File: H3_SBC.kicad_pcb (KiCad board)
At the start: 2 copper layers, 50 x 40 mm, 11 parts, among them CN1 YXT-BB10-50P-02, CN2 YXT-BB10-50P-02, CN3 YXT-BB10-50P-02, J1 HR911105A_C12074, U1 H3, U2 AXP223_C2997893, U3 K4B4G1646E-BYMA 4GB, U4 K4B4G1646E-BYMA 4GB, U5 KLM4G1FETE-B041, U8 XOS32024000LT00351005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

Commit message: changed some ethernet stuff
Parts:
- removed J1: HR911105A_C12074, easyeda2kicad:RJ45-TH_HR911105A
- added RJ1: R-RJ45R08P-C000, easyeda2kicad:RJ45-TH_R-RJ45R08P-C000, F.Cu at (212.5, 79.1)
- added U9: RTL8211E-VB-CG, easyeda2kicad:QFN-48_L6.0-W6.0-P0.40-BL-EP3.8, F.Cu at (190.3, 92.1)
- moved U1 0.14 mm to (176.0, 86.9)
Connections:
- CN2 pad 1: unconnected-(CN2-Pad1) -> ENET_MDI0+
- CN2 pad 10: unconnected-(CN2-Pad10) -> ENET_MDI3+
- CN2 pad 11: unconnected-(CN2-Pad11) -> ENET_MDI3-
- CN2 pad 12: unconnected-(CN2-Pad12) -> GND
- CN2 pad 13: unconnected-(CN2-Pad13) -> ENET_LED1
- CN2 pad 14: unconnected-(CN2-Pad14) -> ENET_LED0
- CN2 pad 15: unconnected-(CN2-Pad15) -> ENET_LED2
- CN2 pad 16: unconnected-(CN2-Pad16) -> GND
- CN2 pad 2: unconnected-(CN2-Pad2) -> ENET_MDI0-
- CN2 pad 3: unconnected-(CN2-Pad3) -> GND
- CN2 pad 4: unconnected-(CN2-Pad4) -> ENET_MDI1+
- CN2 pad 5: unconnected-(CN2-Pad5) -> ENET_MDI1-
- CN2 pad 6: unconnected-(CN2-Pad6) -> GND
- CN2 pad 7: unconnected-(CN2-Pad7) -> ENET_MDI2+
- CN2 pad 8: unconnected-(CN2-Pad8) -> ENET_MDI2-
- CN2 pad 9: unconnected-(CN2-Pad9) -> GND
- CN3 pad 1: unconnected-(CN3-Pad1) -> JTAG_MS
- CN3 pad 10: unconnected-(CN3-Pad10) -> GND
- CN3 pad 11: unconnected-(CN3-Pad11) -> PA8
- CN3 pad 12: unconnected-(CN3-Pad12) -> PA9
- CN3 pad 13: unconnected-(CN3-Pad13) -> PA10
- CN3 pad 14: unconnected-(CN3-Pad14) -> GND
- CN3 pad 15: unconnected-(CN3-Pad15) -> TWI0_SCK
- CN3 pad 16: unconnected-(CN3-Pad16) -> TWI0_SDA
- CN3 pad 17: unconnected-(CN3-Pad17) -> GND
- CN3 pad 18: unconnected-(CN3-Pad18) -> UART3_TX
- CN3 pad 19: unconnected-(CN3-Pad19) -> UART3_RX
- CN3 pad 2: unconnected-(CN3-Pad2) -> JTAG_CK
- CN3 pad 20: unconnected-(CN3-Pad20) -> UART3_RTS
- CN3 pad 21: unconnected-(CN3-Pad21) -> UART3_CTS
- CN3 pad 3: unconnected-(CN3-Pad3) -> JTAG_DO
- CN3 pad 4: unconnected-(CN3-Pad4) -> JTAG_DI
- CN3 pad 41: unconnected-(CN3-Pad41) -> SPI0_CS
- CN3 pad 42: unconnected-(CN3-Pad42) -> SPI0_CLK
- CN3 pad 43: unconnected-(CN3-Pad43) -> SPI0_MISO
- CN3 pad 44: unconnected-(CN3-Pad44) -> SPI0_MOSI
- CN3 pad 45: unconnected-(CN3-Pad45) -> GND
- CN3 pad 46: unconnected-(CN3-Pad46) -> PA21
- CN3 pad 47: unconnected-(CN3-Pad47) -> PA20
- CN3 pad 48: unconnected-(CN3-Pad48) -> PA19
- CN3 pad 49: unconnected-(CN3-Pad49) -> PA18
- CN3 pad 5: unconnected-(CN3-Pad5) -> GND
- CN3 pad 50: unconnected-(CN3-Pad50) -> PA17
- CN3 pad 6: unconnected-(CN3-Pad6) -> PA4
- CN3 pad 7: unconnected-(CN3-Pad7) -> PA5
- CN3 pad 8: unconnected-(CN3-Pad8) -> PA6
- CN3 pad 9: unconnected-(CN3-Pad9) -> PA7
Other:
- copper layers 2 -> 6

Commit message: switched eMMC
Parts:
- removed U5: KLM4G1FETE-B041, easyeda2kicad:FBGA-153_L11.0-W10.0-P0.50_KLM4G1FETE-B041
- added U10: XT28EG32GA4YJECGA, easyeda2kicad:VFBGA-153_L13.0-W11.5-P0.50-BL_SKYHIGHMEMORY_S40FC004C1B1I00000, F.Cu at (176.2, 72.3)

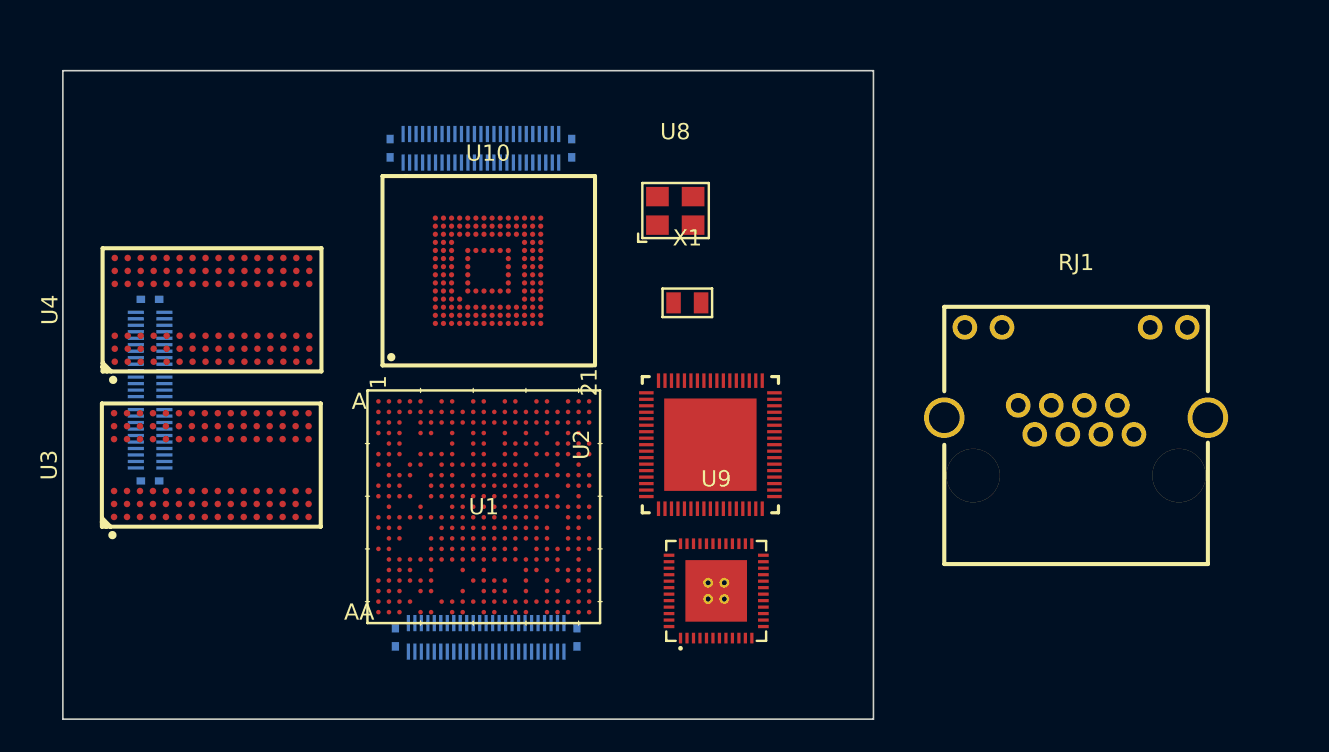
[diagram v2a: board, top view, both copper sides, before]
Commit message: power changes and pinout update
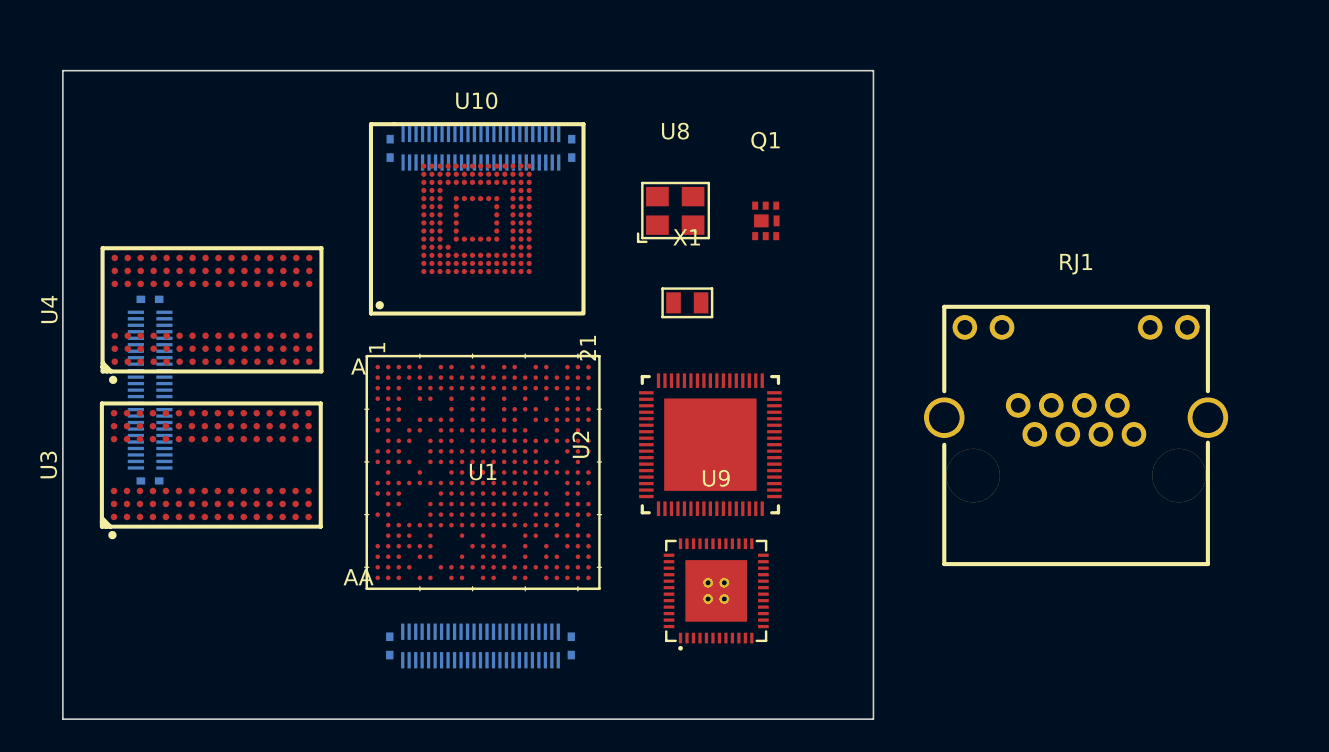
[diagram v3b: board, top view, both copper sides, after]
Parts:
- added Q1: WPM1481-6/TR, easyeda2kicad:DFN-6L_L2.0-W2.0-P0.65-BL_WPM1481-6, F.Cu at (193.4, 69.3)
- moved U10 3.28 mm to (175.5, 69.1)
- moved U1 2.12 mm to (175.9, 84.8)
- moved CN2 0.64 mm to (175.8, 95.5)
- turned CN1 to 0 degrees
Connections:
- CN1 pad 26: unconnected-(CN1-Pad26) -> CHG_LED
- CN1 pad 27: unconnected-(CN1-Pad27) -> PWR_ON
- CN1 pad 28: unconnected-(CN1-Pad28) -> GND
- CN2 pad 41: unconnected-(CN2-Pad41) -> SPI0_CS
- CN2 pad 42: unconnected-(CN2-Pad42) -> SPI0_CLK
- CN2 pad 43: unconnected-(CN2-Pad43) -> SPI0_MISO
- CN2 pad 44: unconnected-(CN2-Pad44) -> SPI0_MOSI
- CN2 pad 45: unconnected-(CN2-Pad45) -> GND
- CN2 pad 46: unconnected-(CN2-Pad46) -> PA21
- CN2 pad 47: unconnected-(CN2-Pad47) -> PA20
- CN2 pad 48: unconnected-(CN2-Pad48) -> PA19
- CN2 pad 49: unconnected-(CN2-Pad49) -> PA18
- CN2 pad 50: unconnected-(CN2-Pad50) -> PA17
- CN3 pad 26: unconnected-(CN3-Pad26) -> AXP_PWROK
- CN3 pad 27: unconnected-(CN3-Pad27) -> PWR_ON
- CN3 pad 28: unconnected-(CN3-Pad28) -> ELDO3
- CN3 pad 29: unconnected-(CN3-Pad29) -> ELDO3
- CN3 pad 30: unconnected-(CN3-Pad30) -> ELDO2
- CN3 pad 31: unconnected-(CN3-Pad31) -> ELDO2
- CN3 pad 32: unconnected-(CN3-Pad32) -> ELDO1
- CN3 pad 33: unconnected-(CN3-Pad33) -> ELDO1
- CN3 pad 34: unconnected-(CN3-Pad34) -> NTC
- CN3 pad 35: unconnected-(CN3-Pad35) -> DLDO4
- CN3 pad 36: unconnected-(CN3-Pad36) -> DLDO4
- CN3 pad 37: unconnected-(CN3-Pad37) -> DLDO3
- CN3 pad 38: unconnected-(CN3-Pad38) -> DLDO3
- CN3 pad 39: unconnected-(CN3-Pad39) -> DLDO2
- CN3 pad 40: unconnected-(CN3-Pad40) -> DLDO2
- CN3 pad 41: SPI0_CS -> DLDO1
- CN3 pad 42: SPI0_CLK -> DLDO1
- CN3 pad 43: SPI0_MISO -> +BATT
- CN3 pad 44: SPI0_MOSI -> +BATT
- CN3 pad 45: GND -> +BATT
- CN3 pad 46: PA21 -> +BATT
- CN3 pad 47: PA20 -> +5V
- CN3 pad 48: PA19 -> +5V
- CN3 pad 49: PA18 -> +5V
- CN3 pad 50: PA17 -> +5V
- U2 pad 1: unconnected-(U2A-ELDOIN-Pad1) -> /Power/IPSOUT
- U2 pad 11: unconnected-(U2A-N_VBUSEN-Pad11) -> VCC_RTC
- U2 pad 12: unconnected-(U2A-PWRON-Pad12) -> PWR_ON
- U2 pad 13: Net-(U2B-VIN1) -> /Power/IPSOUT
- U2 pad 18: unconnected-(U2A-DLDOIN-Pad18) -> /Power/IPSOUT
- U2 pad 2: unconnected-(U2A-ELDO2-Pad2) -> ELDO2
- U2 pad 23: Net-(U2C-VIN2) -> /Power/IPSOUT
- U2 pad 29: unconnected-(U2A-IRQ-Pad29) -> AXP_IRQ
- U2 pad 3: unconnected-(U2A-ELDO3-Pad3) -> ELDO3
- U2 pad 30: unconnected-(U2A-TS-Pad30) -> NTC
- U2 pad 31: unconnected-(U2A-GPIO1/PWREN-Pad31) -> Net-(U2A-GPIO1/PWREN)
- U2 pad 32: unconnected-(U2A-ALDO1-Pad32) -> VCC_3V3_ANALOG
- U2 pad 33: unconnected-(U2A-ALDOIN-Pad33) -> /Power/IPSOUT
- U2 pad 37: unconnected-(U2A-GPIO0-Pad37) -> Net-(U2A-GPIO0)
- U2 pad 39: Net-(U2D-VIN3) -> /Power/IPSOUT
- U2 pad 43: unconnected-(U2A-PWROK-Pad43) -> AXP_PWROK
- U2 pad 44: unconnected-(U2A-SCK-Pad44) -> AXP_SCL
- U2 pad 45: unconnected-(U2A-SDA-Pad45) -> AXP_SDA
- U2 pad 46: Net-(U2A-VCC_RTC) -> VCC_RTC
- U2 pad 49: unconnected-(U2A-BATSENCE-Pad49) -> +BATT
- U2 pad 50: unconnected-(U2A-LOADSENCE-Pad50) -> /Power/CHSENCEN
- U2 pad 51: unconnected-(U2A-N_BATDRV-Pad51) -> /Power/N_BATDRV
- U2 pad 52: unconnected-(U2A-CHGLED-Pad52) -> CHG_LED
- U2 pad 53: unconnected-(U2A-PS-Pad53) -> /Power/IPSOUT
- U2 pad 54: unconnected-(U2A-PS-Pad54) -> /Power/IPSOUT
- U2 pad 57: unconnected-(U2A-CHSENCEP-Pad57) -> /Power/CHSENCEP
- U2 pad 58: unconnected-(U2A-CHSENCEN-Pad58) -> /Power/CHSENCEN
- U2 pad 59: unconnected-(U2A-PGND_CHG-Pad59) -> GND
- U2 pad 60: unconnected-(U2A-LX_CHG-Pad60) -> /Power/LX_CHG
- U2 pad 61: unconnected-(U2A-LX_CHG-Pad61) -> /Power/LX_CHG
- U2 pad 62: unconnected-(U2A-VIN_CHG-Pad62) -> /Power/IPSOUT
- U2 pad 63: unconnected-(U2A-VIN_CHG-Pad63) -> /Power/IPSOUT
- U2 pad 68: unconnected-(U2A-ELDO1-Pad68) -> ELDO1

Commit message: minor changes
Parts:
- moved U1 0.54 mm to (175.9, 85.3)
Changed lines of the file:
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@@
 	(footprint "H3:BGA347_H3_AWT"
 		(layer "F.Cu")
-		(at 175.921601 84.784)
+		(at 175.9192 85.322)
 		(tags "H3 ")
 		(property "Reference" "U1"

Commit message: minor changes
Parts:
- removed RJ1: R-RJ45R08P-C000, easyeda2kicad:RJ45-TH_R-RJ45R08P-C000
- removed U8: XOS32024000LT00351005, easyeda2kicad:OSC-SMD_4P-L3.2-W2.5-BL
- added X2: SMD-5032_4P 24M 20pf, easyeda2kicad:CRYSTAL-SMD_4P-L5.0-W3.2-BL, F.Cu at (188.3, 63.9)
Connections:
- net VCC_3V3_ANALOG renamed VCC3V3_AUDIO
- CN1 pad 18: unconnected-(CN1-Pad18) -> PG0
- CN1 pad 19: unconnected-(CN1-Pad19) -> PG1
- CN1 pad 20: unconnected-(CN1-Pad20) -> PG2
- CN1 pad 21: unconnected-(CN1-Pad21) -> PG3
- CN1 pad 22: unconnected-(CN1-Pad22) -> PG4
- CN1 pad 23: unconnected-(CN1-Pad23) -> PG5
- CN1 pad 24: unconnected-(CN1-Pad24) -> PG6
- CN1 pad 25: unconnected-(CN1-Pad25) -> PG7
- CN2 pad 17: unconnected-(CN2-Pad17) -> UBOOT
- CN2 pad 18: unconnected-(CN2-Pad18) -> GND
- CN2 pad 19: unconnected-(CN2-Pad19) -> PG8
- CN2 pad 20: unconnected-(CN2-Pad20) -> PG9
- CN2 pad 21: unconnected-(CN2-Pad21) -> GND
- CN2 pad 22: unconnected-(CN2-Pad22) -> DCDC4
- CN2 pad 23: unconnected-(CN2-Pad23) -> DCDC4
- CN2 pad 24: unconnected-(CN2-Pad24) -> DCDC4
- CN2 pad 25: unconnected-(CN2-Pad25) -> DCDC4
- CN2 pad 37: unconnected-(CN2-Pad37) -> GND
- CN2 pad 38: unconnected-(CN2-Pad38) -> PG11
- CN2 pad 39: unconnected-(CN2-Pad39) -> PG10
- CN2 pad 40: unconnected-(CN2-Pad40) -> GND
- CN3 pad 22: unconnected-(CN3-Pad22) -> GND
- CN3 pad 23: unconnected-(CN3-Pad23) -> TVOUT
- CN3 pad 24: unconnected-(CN3-Pad24) -> GND
- CN3 pad 25: unconnected-(CN3-Pad25) -> GND
- U2 pad 28: VCC1V2_CPU -> CPUX_FB
- U2 pad 64: unconnected-(U2E-VIN4-Pad64) -> /Power/IPSOUT
- U2 pad 65: unconnected-(U2E-LX4-Pad65) -> Net-(U2E-LX4)
- U2 pad 66: unconnected-(U2E-PGND4-Pad66) -> GND
- U2 pad 67: unconnected-(U2E-DCDC4-Pad67) -> DCDC4
